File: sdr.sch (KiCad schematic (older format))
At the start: 0 parts

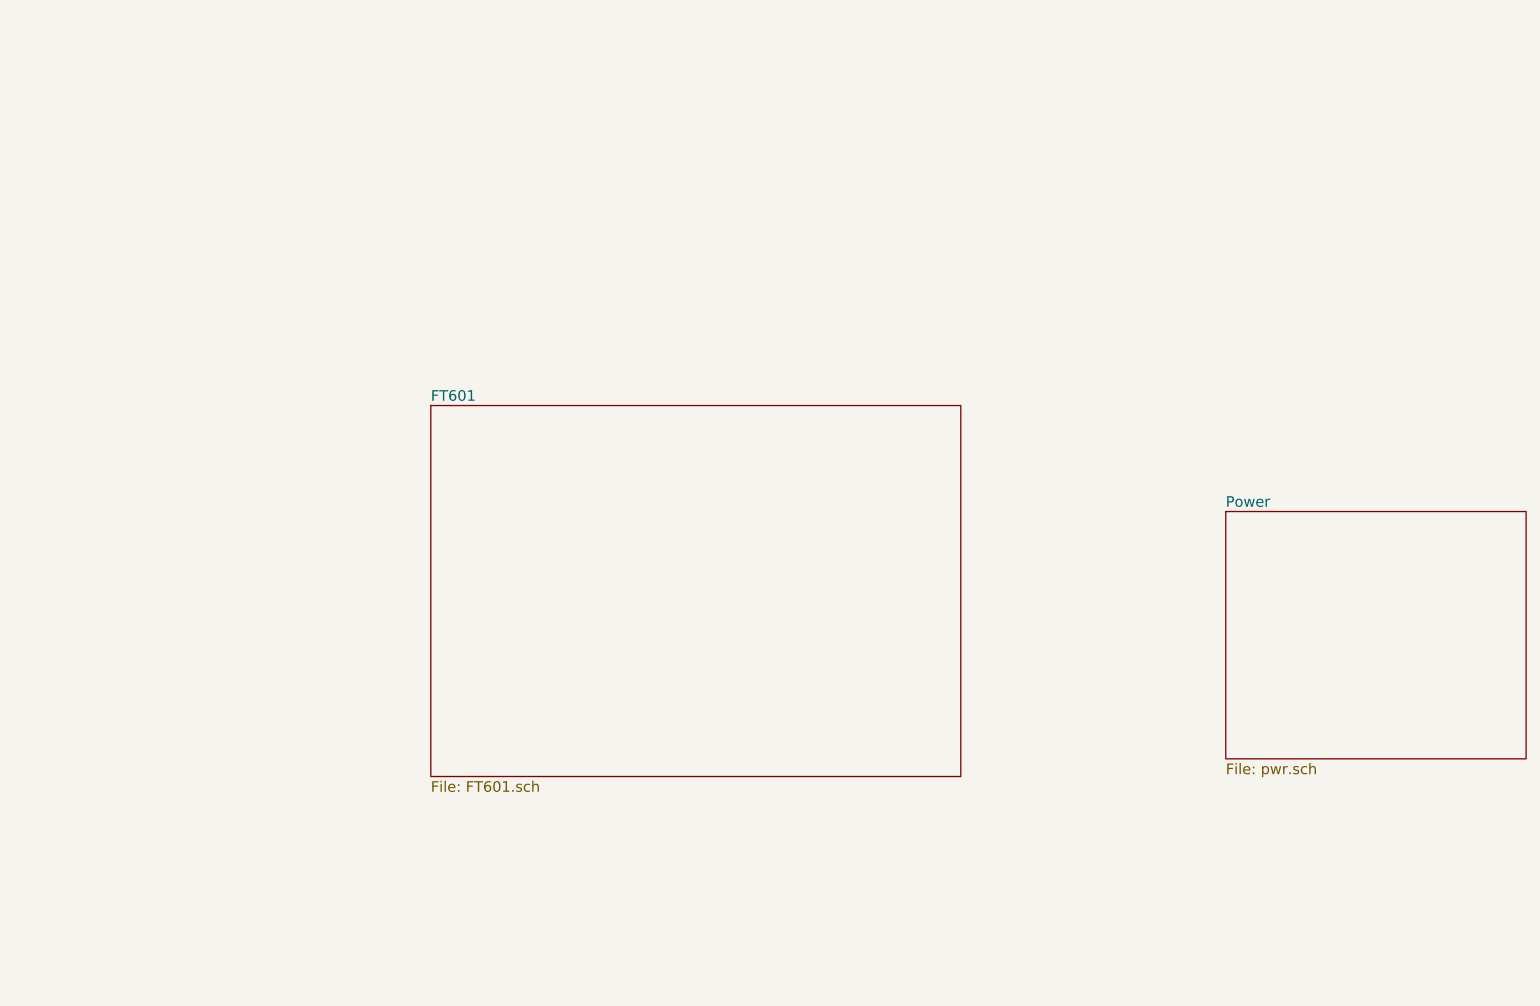
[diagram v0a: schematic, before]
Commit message: Cloack, LMS are added
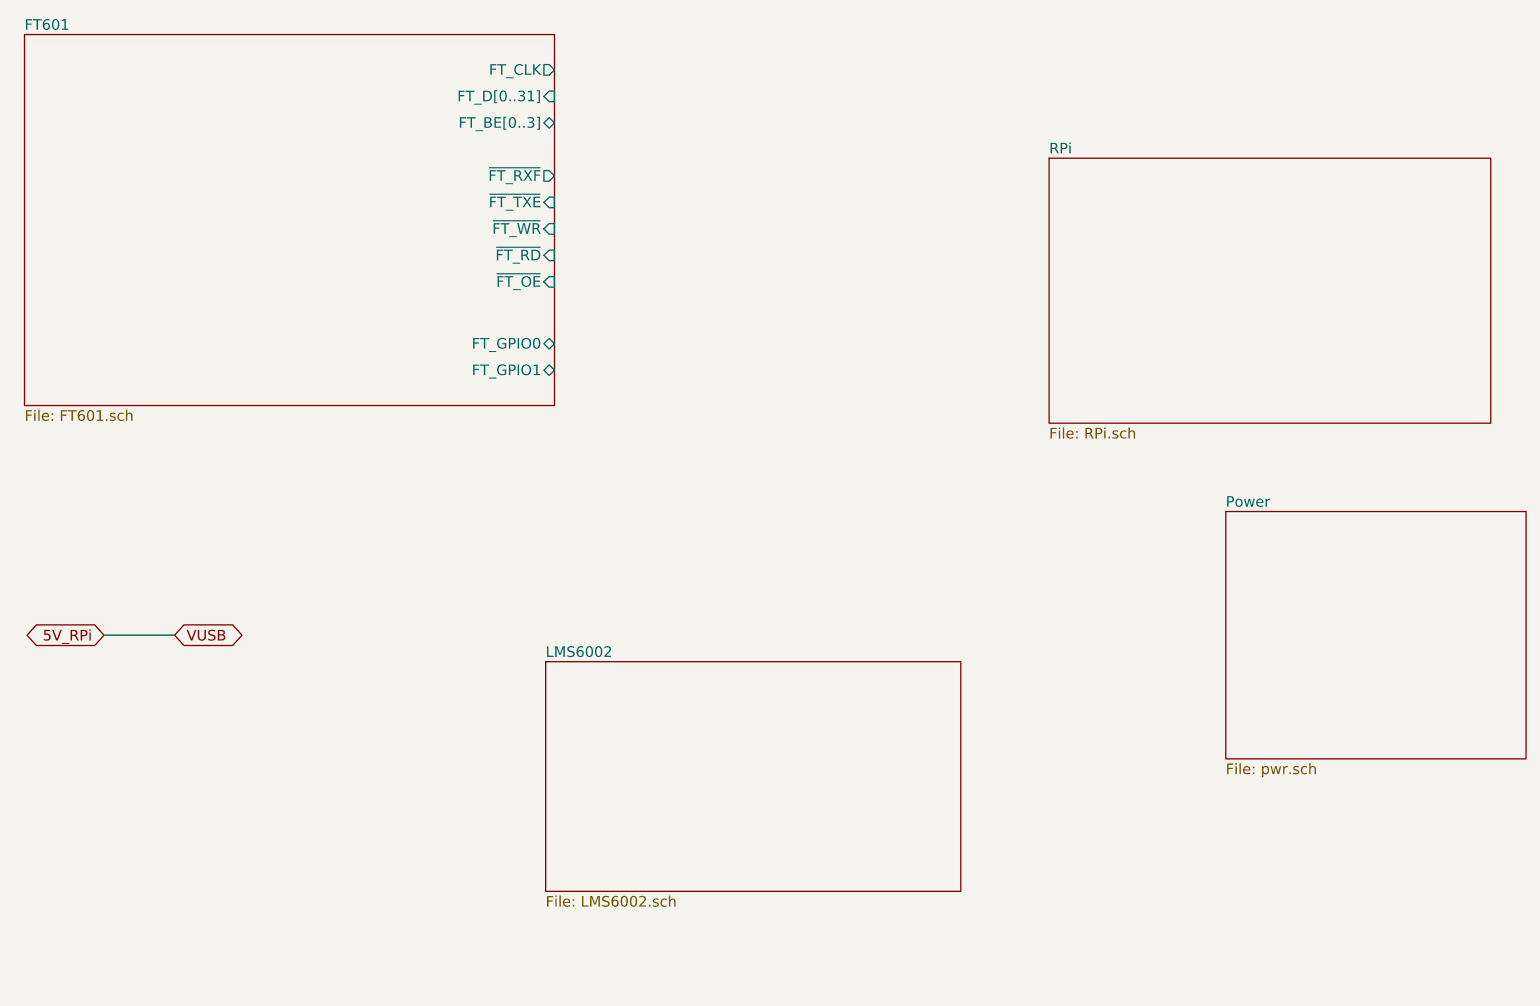
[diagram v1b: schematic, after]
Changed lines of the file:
@@
 EESchema Schematic File Version 2
+LIBS:sdr-rescue
 LIBS:power
 LIBS:device
@@
 LIBS:sdr
 LIBS:usb-type-c
+LIBS:sdr-cache
 EELAYER 25 0
 EELAYER END
 $Descr A4 11693 8268
 encoding utf-8
-Sheet 1 3
+Sheet 1 5
 Title ""
 Date ""
@@
 $EndSheet
 $Sheet
-S 3800 3400 3000 2100
+S 1500 1300 3000 2100
 U 5896CA7C
 F0 "FT601" 60
 F1 "FT601.sch" 60
+F2 "FT_D[0..31]" I R 4500 1650 60
+F3 "~FT_TXE" I R 4500 2250 60
+F4 "~FT_RXF" O R 4500 2100 60
+F5 "~FT_WR" I R 4500 2400 60
+F6 "~FT_RD" I R 4500 2550 60
+F7 "~FT_OE" I R 4500 2700 60
+F8 "FT_GPIO0" B R 4500 3050 60
+F9 "FT_GPIO1" B R 4500 3200 60
+F10 "FT_CLK" O R 4500 1500 60
+F11 "FT_BE[0..3]" B R 4500 1800 60
+$EndSheet
+$Sheet
+S 7300 2000 2500 1500
+U 589F831F
+F0 "RPi" 60
+F1 "RPi.sch" 60
+$EndSheet
+Text GLabel 1950 4700 0    60   BiDi ~ 0
+5V_RPi
+Text GLabel 2350 4700 2    60   BiDi ~ 0
+VUSB
+Wire Wire Line
+	1950 4700 2350 4700
+$Sheet
+S 4450 4850 2350 1300
+U 58A034EC
+F0 "LMS6002" 60
+F1 "LMS6002.sch" 60
 $EndSheet
 $EndSCHEMATC

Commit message: Schematic is done except RF.
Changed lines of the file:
@@
 $Descr A4 11693 8268
 encoding utf-8
-Sheet 1 5
-Title ""
+Sheet 1 6
+Title "SDR"
 Date ""
 Rev ""
-Comp ""
+Comp "Dmitry Kuznetsov"
 Comment1 ""
 Comment2 ""
@@
 $EndSheet
 $Sheet
-S 1500 1300 3000 2100
-U 5896CA7C
-F0 "FT601" 60
-F1 "FT601.sch" 60
-F2 "FT_D[0..31]" I R 4500 1650 60
-F3 "~FT_TXE" I R 4500 2250 60
-F4 "~FT_RXF" O R 4500 2100 60
-F5 "~FT_WR" I R 4500 2400 60
-F6 "~FT_RD" I R 4500 2550 60
-F7 "~FT_OE" I R 4500 2700 60
-F8 "FT_GPIO0" B R 4500 3050 60
-F9 "FT_GPIO1" B R 4500 3200 60
-F10 "FT_CLK" O R 4500 1500 60
-F11 "FT_BE[0..3]" B R 4500 1800 60
-$EndSheet
-$Sheet
 S 7300 2000 2500 1500
 U 589F831F
@@
 F1 "RPi.sch" 60
 $EndSheet
-Text GLabel 1950 4700 0    60   BiDi ~ 0
-5V_RPi
-Text GLabel 2350 4700 2    60   BiDi ~ 0
-VUSB
-Wire Wire Line
-	1950 4700 2350 4700
 $Sheet
 S 4450 4850 2350 1300
@@
 F1 "LMS6002.sch" 60
 $EndSheet
+$Sheet
+S 1500 1300 3000 2100
+U 5896CA7C
+F0 "FT601" 60
+F1 "FT601.sch" 60
+$EndSheet
+$Sheet
+S 1750 4500 2300 2100
+U 58A3C5E2
+F0 "Power2" 60
+F1 "power2.sch" 60
+$EndSheet
 $EndSCHEMATC

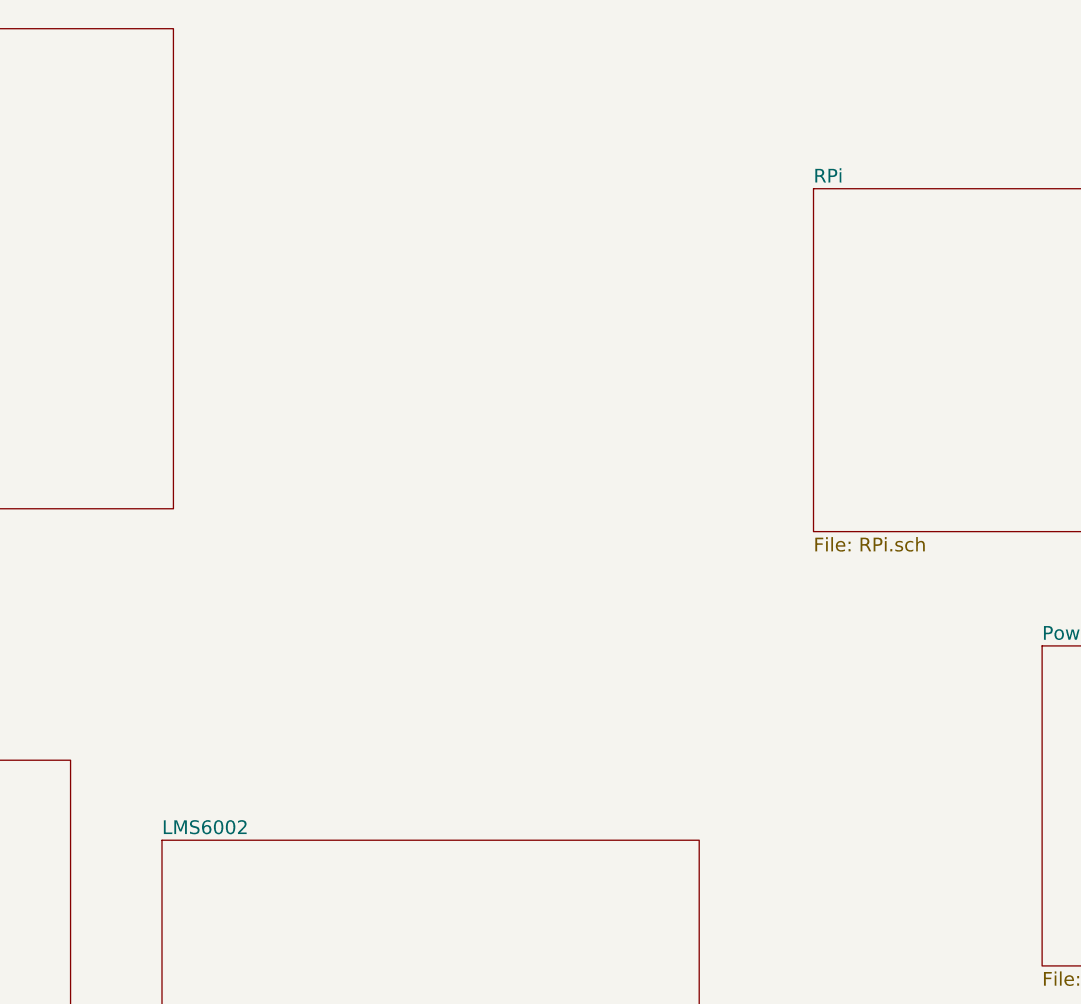
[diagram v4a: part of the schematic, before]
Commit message: Preliminary placing top layer of RF
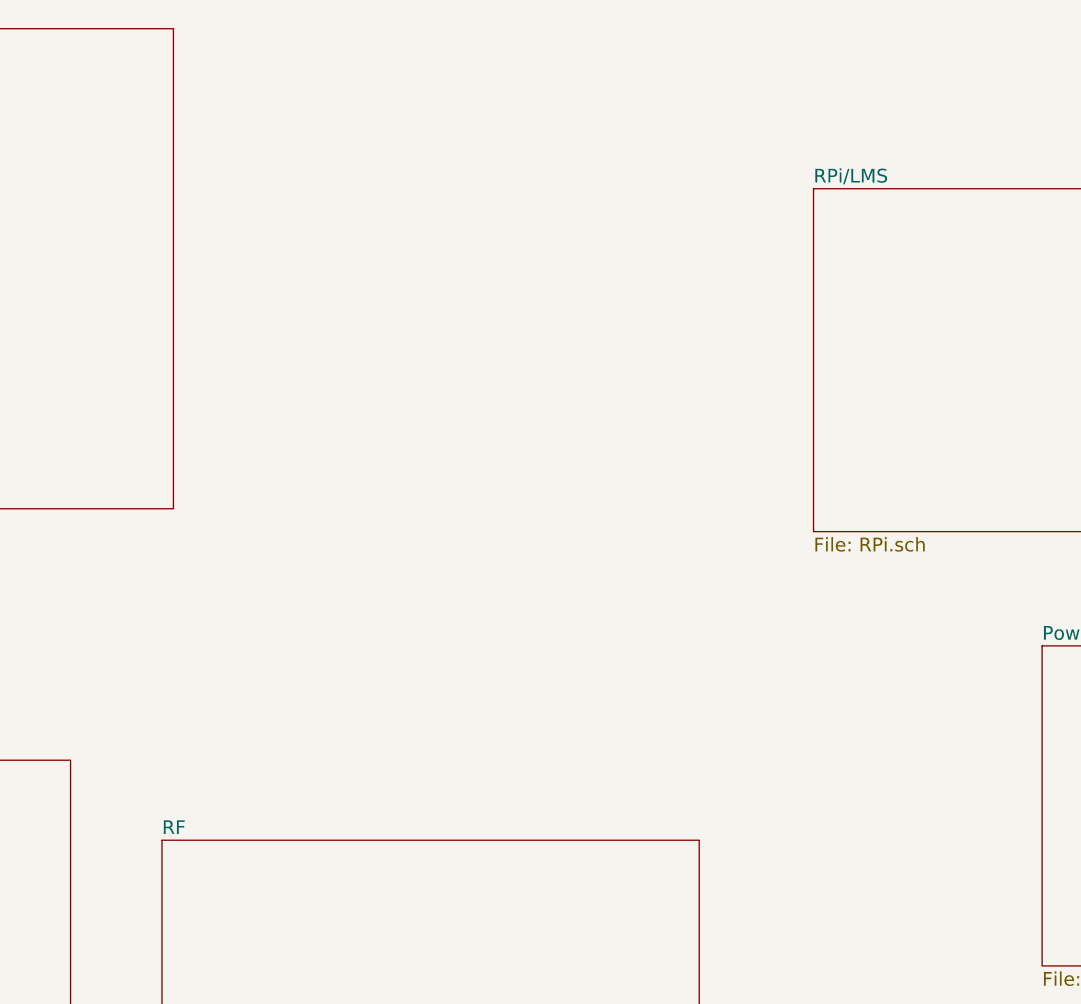
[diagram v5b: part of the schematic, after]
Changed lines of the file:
@@
 S 7300 2000 2500 1500
 U 589F831F
-F0 "RPi" 60
+F0 "RPi/LMS" 60
 F1 "RPi.sch" 60
 $EndSheet
@@
 S 4450 4850 2350 1300
 U 58A034EC
-F0 "LMS6002" 60
+F0 "RF" 60
 F1 "LMS6002.sch" 60
 $EndSheet
